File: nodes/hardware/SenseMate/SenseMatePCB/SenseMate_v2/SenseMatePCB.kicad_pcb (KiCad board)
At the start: 2 copper layers, 28.2 x 57.5 mm, 21 parts, among them J1 Conn_01x04, M1 Motor_DC, Q1 2SC1815, Q2 2SC1815, SW5 SW_DPDT_x2, U1 XIAO-nRF52840-Plus-SMD, U2 RFM95W-868S2

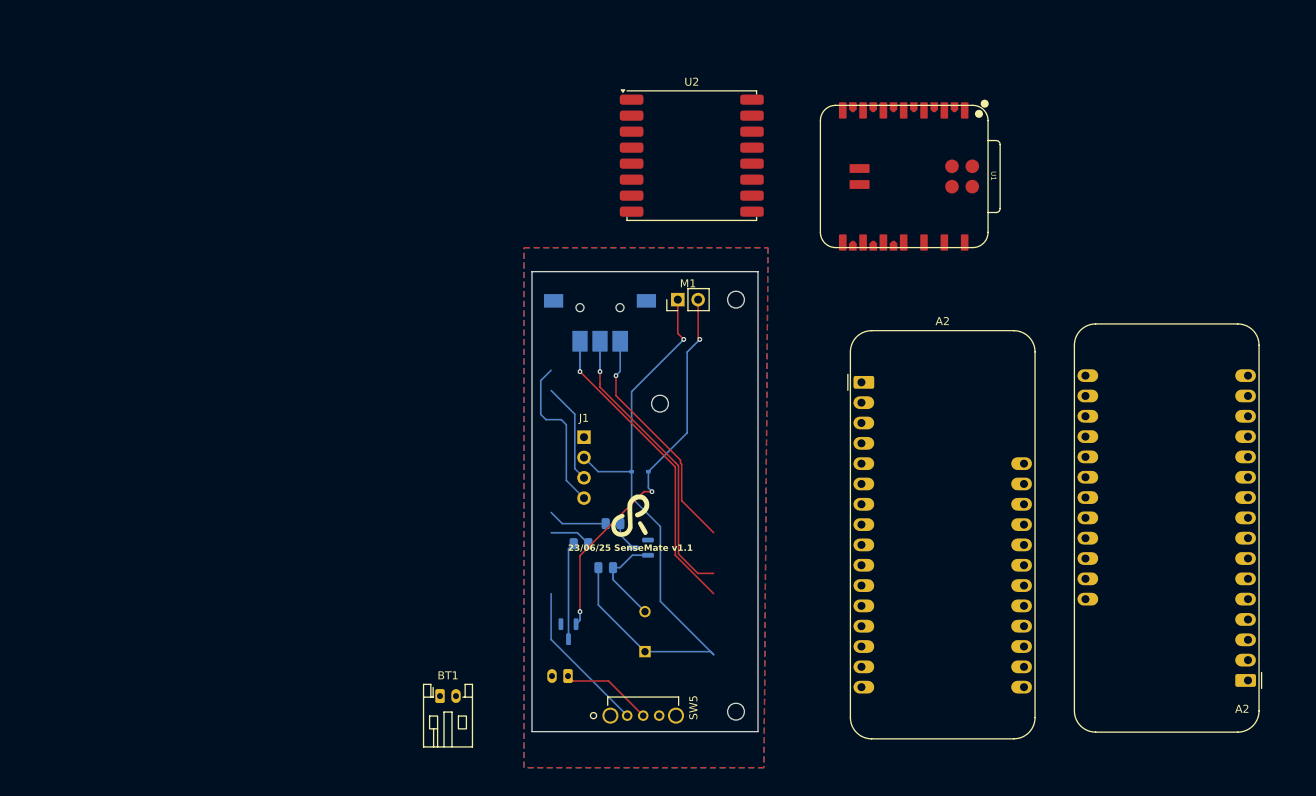
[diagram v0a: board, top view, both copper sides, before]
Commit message: 26-finished marking used pins
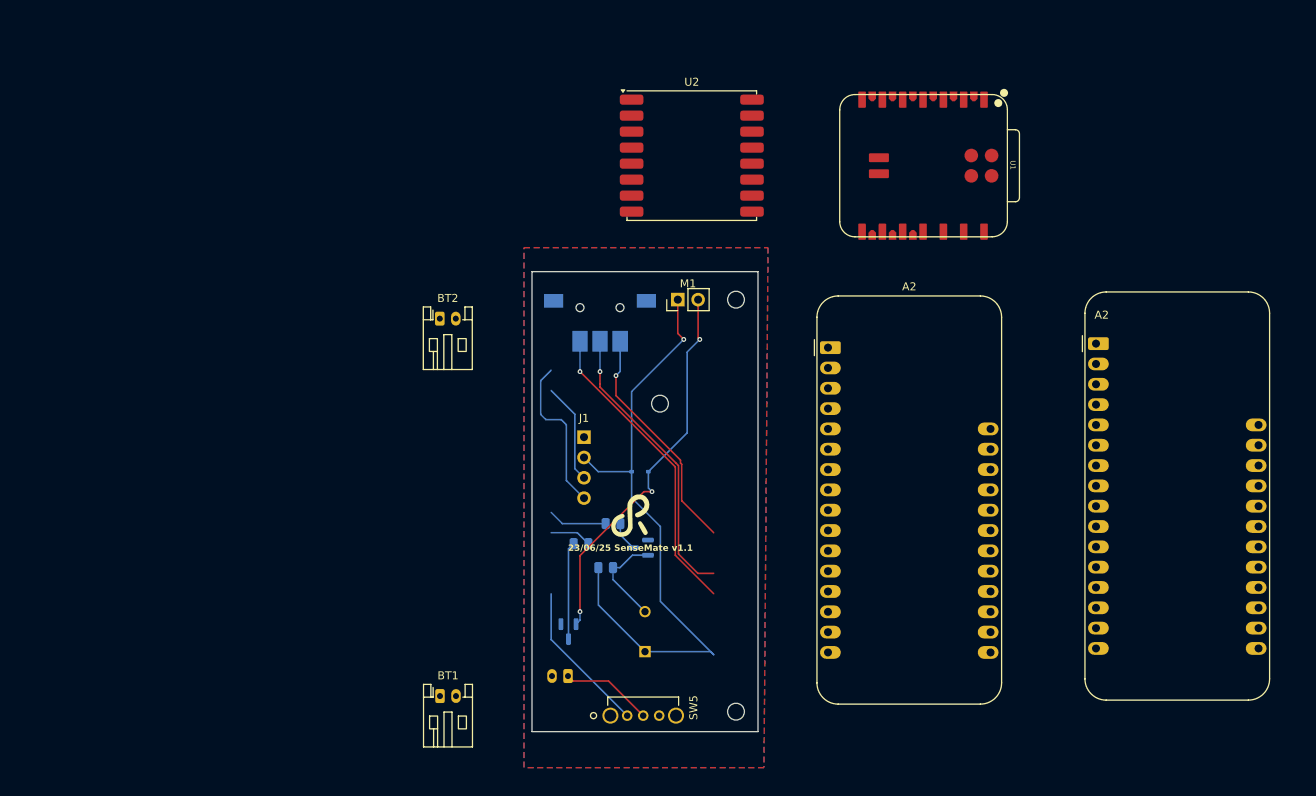
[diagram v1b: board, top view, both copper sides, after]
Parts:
- added BT2: Battery, Connector_JST:JST_PH_S2B-PH-K_1x02_P2.00mm_Horizontal, F.Cu at (81.5, 60.9)
- U1: footprint XIAO:XIAO-nRF52840-Plus-SMD -> SenseMateLibrary:XIAO-nRF52840-Plus-SMD
- moved A2 46.2 mm to (163.5, 64.0), turned to 0 degrees
- moved A2 6.03 mm to (130.0, 64.5)
- moved U1 2.77 mm to (141.9, 41.8)
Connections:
- U1 pad 10: unconnected-(U1-P1.14_D9_MISO-Pad10) -> LoRa_MISO
- U1 pad 11: unconnected-(U1-P1.15_D10_MOSI-Pad11) -> LoRa_MOSI
- U1 pad 12: unconnected-(U1-3V3-Pad12) -> +3V3
- U1 pad 26: unconnected-(U1-REST-Pad26) -> LoRa_RST
- U1 pad 9: unconnected-(U1-P1.13_D8_SCK-Pad9) -> LoRa_SCK
- U2 pad 15: unconnected-(U2-DIO1-Pad15) -> LoRa_DIO1
- U2 pad 16: unconnected-(U2-DIO2-Pad16) -> LoRa_DIO2
- U2 pad 2: unconnected-(U2-MISO-Pad2) -> LoRa_MISO
- U2 pad 3: unconnected-(U2-MOSI-Pad3) -> LoRa_MOSI
- U2 pad 4: unconnected-(U2-SCK-Pad4) -> LoRa_SCK
- U2 pad 6: unconnected-(U2-RESET-Pad6) -> LoRa_RST

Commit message: 26-Finalisierung der Verbindunen zwischen den Geräten und Aufräumen des Schemas
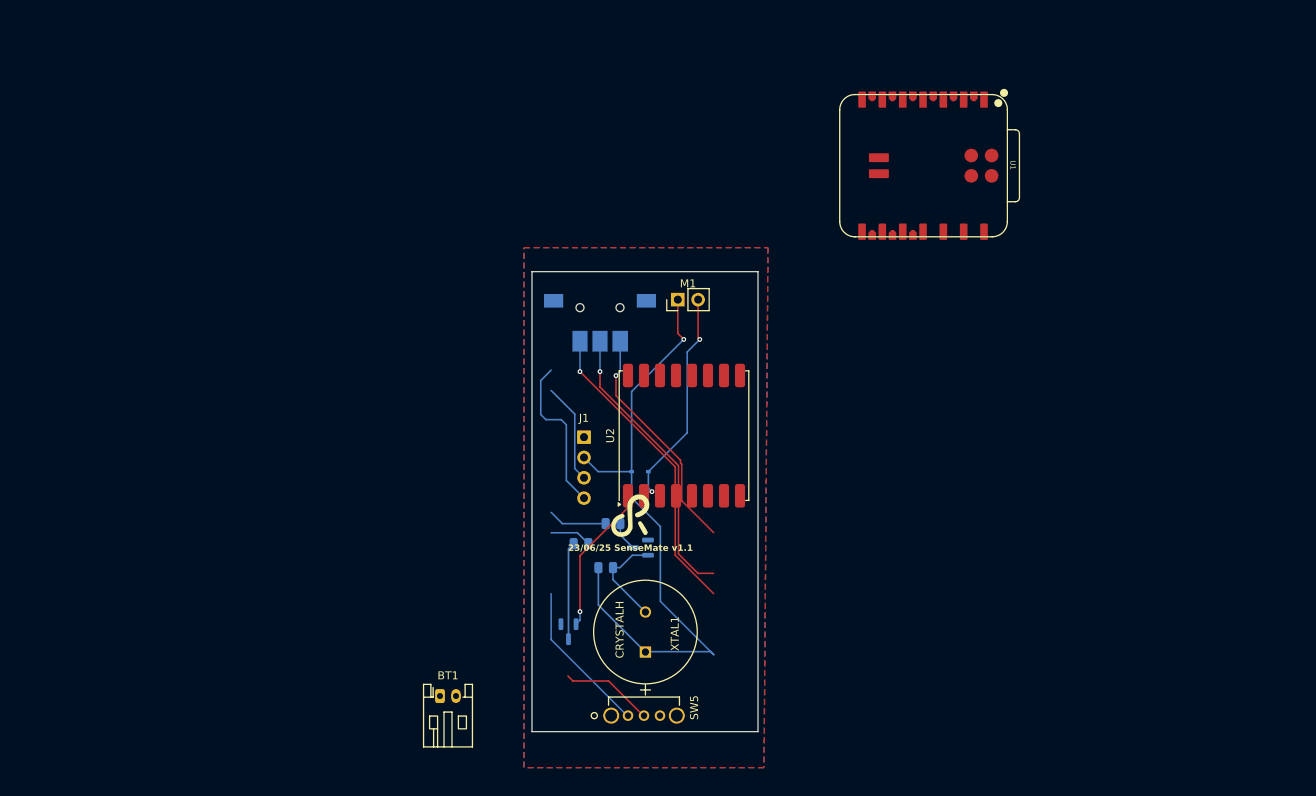
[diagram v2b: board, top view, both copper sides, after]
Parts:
- removed A2 (x2): Adafruit_Feather_Generic, SenseMateLibrary:Adafruit_Feather_Sense
- removed the BT1 at (97.5, 105.5)
- removed BT2: Battery, Connector_JST:JST_PH_S2B-PH-K_1x02_P2.00mm_Horizontal
- removed REF** (x3): MountingHole_2.1mm, MountingHole:MountingHole_2.1mm
- SW5: footprint SenseMate_Pwr_Button_:OS102011MA1QN1 -> SenseMateLibrary:OS102011MA1QN1
- XTAL1: footprint SenseMate_sound:PS1240P02BT -> SenseMateLibrary:PS1240P02BT; moved to F.Cu
- moved U2 35.0 mm to (112.0, 75.5), turned to 90 degrees
- moved SW5 0.10 mm to (105.0, 110.5)
- moved XTAL1 0.07 mm to (107.2, 102.5)
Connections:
- J1 pad 3: Net-(A2-SCL) -> SCL
- J1 pad 4: Net-(A2-SDA) -> SDA
- R2 pad 2: Net-(A2-12) -> BUZ_EN
- R3 pad 2: Net-(A2-13) -> VIB_EN
- S1 pad 1: Net-(A2-A3) -> TMB1
- S1 pad 2: Net-(A2-A0) -> TMB2
- S1 pad T1: Net-(A2-A1) -> TMBT1
- SW5 pad 1: Net-(A2-VBAT) -> VBAT
- U1 pad 13: unconnected-(U1-GND-Pad13) -> GND
- U1 pad 26: LoRa_RST -> unconnected-(U1-REST-Pad26)
- U1 pad 27: unconnected-(U1-GND-Pad27) -> GND
- U1 pad 28: unconnected-(U1-VBAT-Pad28) -> VBAT
- U1 pad 29: unconnected-(U1-GND-Pad29) -> GND
- U1 pad 5: unconnected-(U1-P0.04_A4_D4_SDA-Pad5) -> SDA
- U1 pad 6: unconnected-(U1-P0.05_A5_D5_SCL-Pad6) -> SCL
- U2 pad 14: unconnected-(U2-DIO0-Pad14) -> LoRa_DIO0
- U2 pad 5: unconnected-(U2-NSS-Pad5) -> LoRa_NSS
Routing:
- net TMB2: track 0.00 -> 38.5 mm, vias 0 -> 1
- net Net-(A2-A0): track 38.5 -> 0.00 mm, vias 1 -> 0
- net TMBT1: track 0.00 -> 36.1 mm, vias 0 -> 1
- net Net-(A2-A1): track 36.1 -> 0.00 mm, vias 1 -> 0
- net TMB1: track 0.00 -> 29.2 mm, vias 0 -> 1
- net Net-(A2-A3): track 29.2 -> 0.00 mm, vias 1 -> 0
- net SDA: track 0.00 -> 19.9 mm
- net Net-(A2-SDA): track 19.9 -> 0.00 mm
- net VBAT: track 0.00 -> 19.2 mm
- net Net-(A2-VBAT): track 19.2 -> 0.00 mm
- net SCL: track 0.00 -> 12.6 mm
- net Net-(A2-SCL): track 12.6 -> 0.00 mm
- net Net-(A2-12): track 7.40 -> 0.00 mm
- net BUZ_EN: track 0.00 -> 7.40 mm
- net VIB_EN: track 0.00 -> 5.21 mm
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
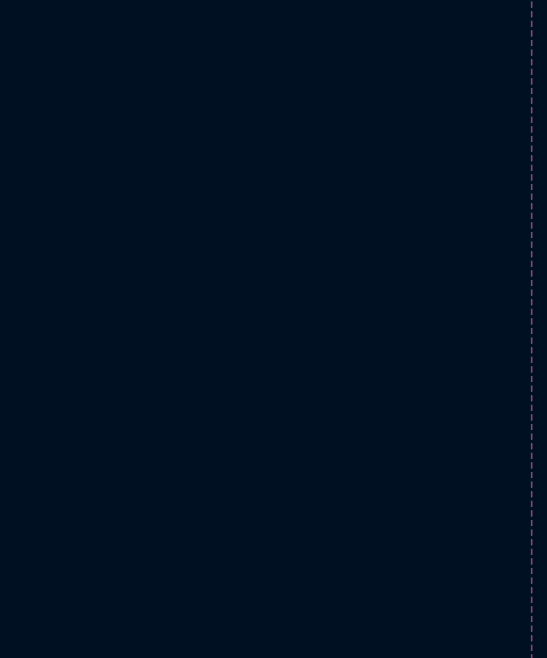
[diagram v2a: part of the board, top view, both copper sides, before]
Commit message: fehlende 3D symboly für SeedStudio und LoraChip hinzugefügt, Netzte Verbunden, Kommentare ergänzt
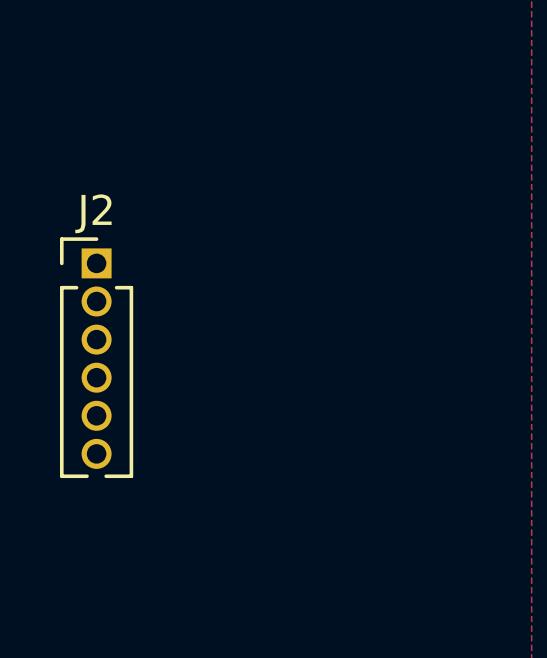
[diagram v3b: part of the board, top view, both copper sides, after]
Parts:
- added J2: Conn_02x06_Counter_Clockwise (PogoPin), Connector_PinHeader_1.27mm:PinHeader_1x06_P1.27mm_Vertical, F.Cu at (77.5, 82.3)
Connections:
- U1 pad 15: unconnected-(U1-P0.15_D11_I2S_SD-Pad15) -> LoRa_DIO0
- U1 pad 16: unconnected-(U1-P0.19_D12_I2S_SCK-Pad16) -> TMB1
- U1 pad 17: unconnected-(U1-P1.01_D13_I2S_WS-Pad17) -> TMB2
- U1 pad 18: unconnected-(U1-P0.09_D14_NFC1_RX1-Pad18) -> Pogo Pins
- U1 pad 19: unconnected-(U1-P0.10_D15_NFC2_TX1-Pad19) -> TMBT1
- U1 pad 2: unconnected-(U1-P0.03_A1_D1-Pad2) -> LoRa_RST
- U1 pad 21: unconnected-(U1-P1.03_D17_SCK1-Pad21) -> VIB_EN
- U1 pad 3: unconnected-(U1-P0.28_A2_D2-Pad3) -> LoRa_DIO1
- U1 pad 4: unconnected-(U1-P0.29_A3_D3-Pad4) -> LoRa_DIO2
- U1 pad 7: unconnected-(U1-P1.11_D6_TX-Pad7) -> LoRa_NSS
- U1 pad 8: unconnected-(U1-P1.12_D7_RX-Pad8) -> BUZ_EN

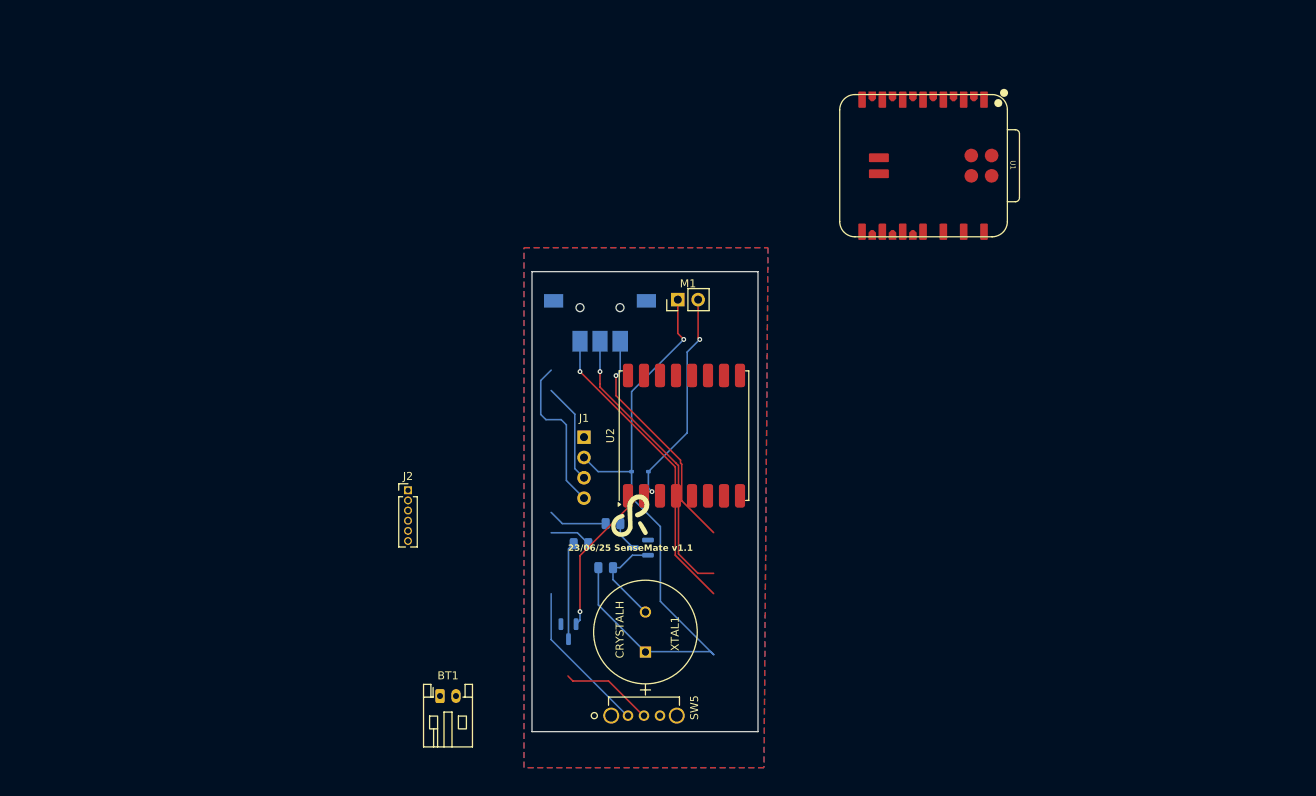
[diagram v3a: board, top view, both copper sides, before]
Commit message: reorganized design of board
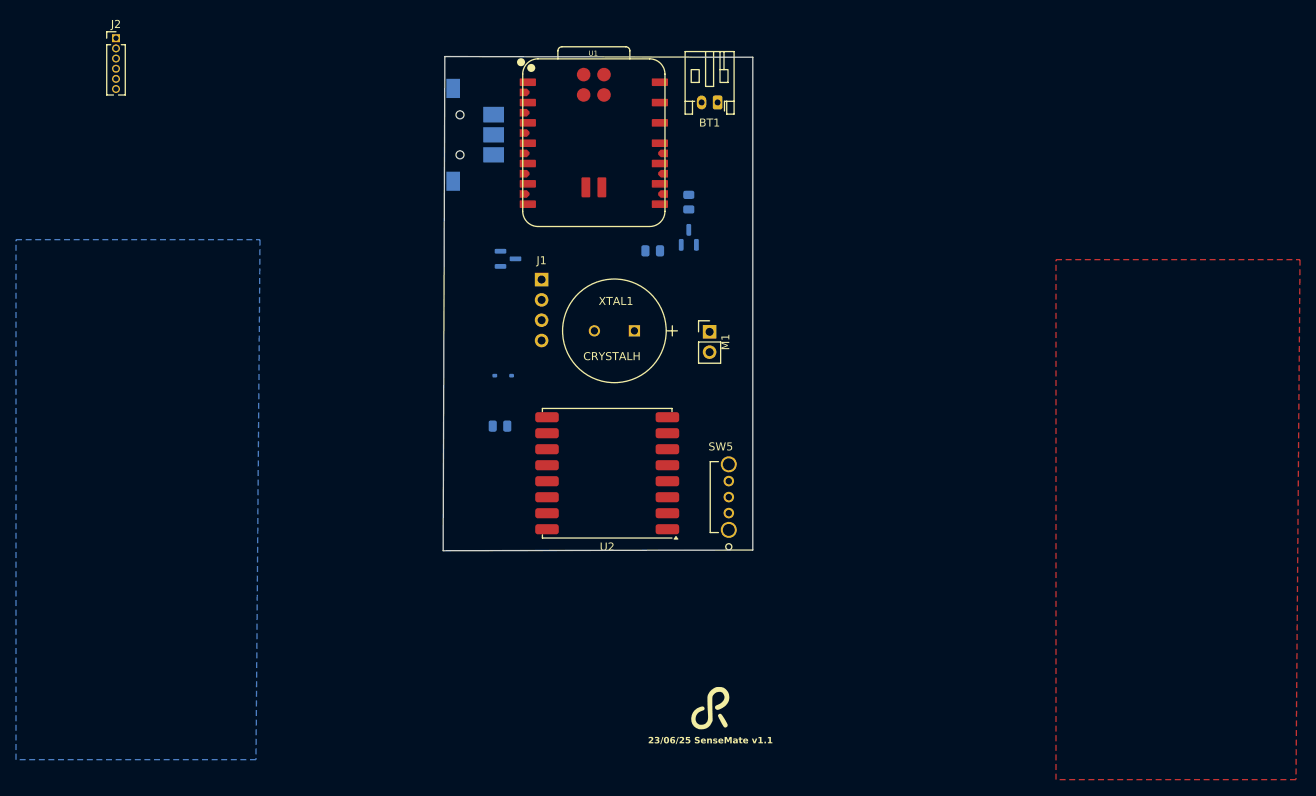
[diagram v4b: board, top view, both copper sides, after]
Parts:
- moved BT1 81.9 mm to (116.2, 33.9), turned to 180 degrees
- moved J2 67.3 mm to (41.0, 25.8)
- moved Q2 51.5 mm to (112.6, 50.7), turned to 90 degrees
- moved R3 44.8 mm to (112.6, 46.3), turned to 90 degrees
- moved U1 41.2 mm to (100.7, 38.9), turned to 90 degrees
- moved XTAL1 40.2 mm to (105.8, 62.4), turned to 180 degrees
- moved Q1 39.7 mm to (90.0, 53.4), turned to 0 degrees
- moved R2 34.5 mm to (108.1, 52.4), turned to 0 degrees
- moved SW5 28.3 mm to (117.6, 85.2), turned to 90 degrees
- moved S1 27.8 mm to (84.0, 37.9), turned to -90 degrees
- moved G*** 26.1 mm to (117.8, 109.6)
- moved R1 22.1 mm to (89.0, 74.3)
- moved D1 20.9 mm to (89.4, 68.0)
- moved J1 20.4 mm to (94.2, 56.0)
- moved U2 10.7 mm to (102.4, 80.2), turned to 180 degrees
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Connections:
- U1 pad 17: TMB2 -> TMBT1
- U1 pad 19: TMBT1 -> TMB2
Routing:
- net +3V3: track 80.0 -> 0.00 mm, vias 1 -> 0
- net Net-(D1-A): track 48.0 -> 0.00 mm, vias 3 -> 0
- net TMB2: track 38.5 -> 0.00 mm, vias 1 -> 0
- net TMBT1: track 36.1 -> 0.00 mm, vias 1 -> 0
- net TMB1: track 29.2 -> 0.00 mm, vias 1 -> 0
- net SDA: track 19.9 -> 0.00 mm
- net VBAT: track 19.2 -> 0.00 mm
- net SCL: track 12.6 -> 0.00 mm
- net Net-(Q2-B): track 12.2 -> 0.00 mm
- net Net-(Q1-C): track 12.2 -> 0.00 mm
- net Net-(BT1-+): track 11.5 -> 0.00 mm
- net BUZ_EN: track 7.40 -> 0.00 mm
- net VIB_EN: track 5.21 -> 0.00 mm
- net Net-(Q1-B): track 3.66 -> 0.00 mm
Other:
- board size 28.2 x 57.5 mm -> 38.7 x 61.8 mm
